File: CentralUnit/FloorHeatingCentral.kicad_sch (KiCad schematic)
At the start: 26 parts, among them J1 Screw_Terminal_01x02, J2 Conn_02x05_Odd_Even, J3 Conn_01x20, Q1 Q_NMOS_GDS, U1 ESP32-DevKitC, U2 74HC595D_118, U3 74HC595D_118, U4 RFM69-ATSHA-breakout, U5 MP1584, U6 LM1117-5.0

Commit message: More cleanup and potentially final routing
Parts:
- J2: footprint (none) -> Connector_IDC:IDC-Header_2x05_P2.54mm_Vertical
- JP1: value (none) -> Jumper_2_Open; footprint (none) -> TestPoint:TestPoint_2Pads_Pitch2.54mm_Drill0.8mm
- U2, U3: footprint digikey-footprints:SOIC-16_W3.90mm -> (none); symbol FloorHeatingCentral-rescue:74HC595D_118-dk_Logic-Shift-Registers -> 74xx:74HC595
- U4: footprint (none) -> RFM69HCW_ATSHA204A_Breakout:RFM69HCW_ATSHA204A_Breakout
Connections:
- net +24V: now also J1.2 (Pin_2); no longer J1.1 (Pin_1)
- net DL_SW: now also U1.24 (ADC2_CH2/*GPIO2); no longer U1.26 (ADC2_CH0/GPIO4)
- net GND: now also J1.1 (Pin_1); no longer J1.2 (Pin_2)
- net at U2.9 (QH'): now also U3.14 (SER)
- net ATSHA: now reaches U4.16 (ATSHA)
- net ATSHA: now also U1.26 (ADC2_CH0/GPIO4)
- no-connect marks 43 -> 42
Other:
- moved on the sheet: C1, C2, J1, U2, U3

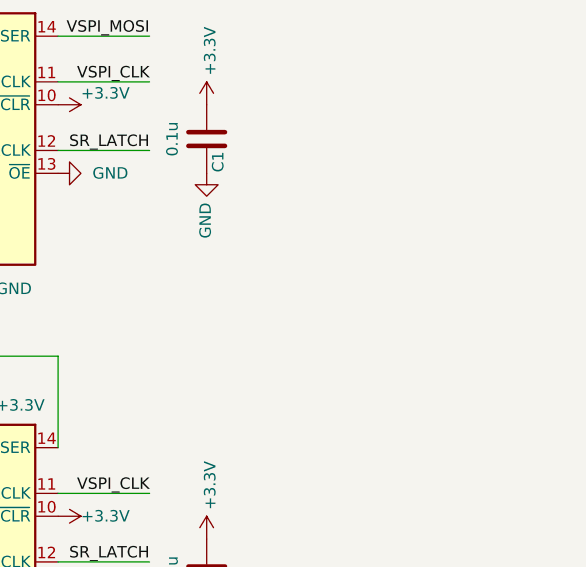
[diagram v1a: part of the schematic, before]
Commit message: Added power port for thermostats
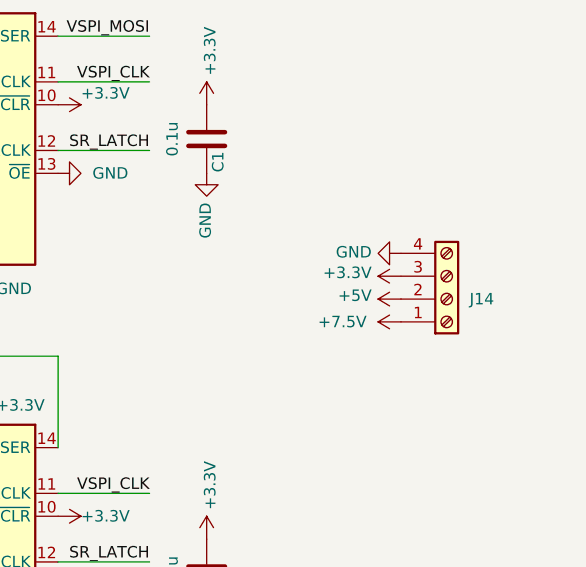
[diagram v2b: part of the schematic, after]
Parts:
- added J14: (no value), symbol Connector:Screw_Terminal_01x04
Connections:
- net +3V3: now also J14.3 (Pin_3)
- net +5V: now also J14.2 (Pin_2)
- net +7.5V: now also J14.1 (Pin_1)
- net GND: now also J14.4 (Pin_4)
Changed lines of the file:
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@@
+    (pin "1")
+  )
+  (symbol (lib_id "power:+7.5V") (at 269.24 78.74 90) (unit 1)
+    (in_bom yes) (on_board yes) (fields_autoplaced)
+    (property "Reference" "#PWR0103" (id 0) (at 273.05 78.74 0)
+      (effects (font (size 1.27 1.27)) hide)
+    )
+    (property "Value" "+7.5V" (id 1) (at 265.43 78.7399 90)
+      (effects (font (size 1.27 1.27)) (justify left))
+    )
+    (property "Footprint" "" (id 2) (at 269.24 78.74 0)
+      (effects (font (size 1.27 1.27)) hide)
+    )
+    (property "Datasheet" "" (id 3) (at 269.24 78.74 0)
+      (effects (font (size 1.27 1.27)) hide)
+    )
     (pin "1")
   )
@@
     (pin "1")
   )
+  (symbol (lib_id "power:+3.3V") (at 269.24 73.66 90) (unit 1)
+    (in_bom yes) (on_board yes)
+    (property "Reference" "#PWR0102" (id 0) (at 273.05 73.66 0)
+      (effects (font (size 1.27 1.27)) hide)
+    )
+    (property "Value" "+3.3V" (id 1) (at 265.9888 73.279 90)
+      (effects (font (size 1.27 1.27)) (justify left))
+    )
+    (property "Footprint" "" (id 2) (at 269.24 73.66 0)
+      (effects (font (size 1.27 1.27)) hide)
+    )
+    (property "Datasheet" "" (id 3) (at 269.24 73.66 0)
+      (effects (font (size 1.27 1.27)) hide)
+    )
+    (pin "1")
+  )
   (symbol (lib_id "power:GND") (at 105.41 50.8 90) (unit 1)
     (in_bom yes) (on_board yes)
@@
     (pin "1")
     (pin "2")
+  )
+  (symbol (lib_id "Connector:Screw_Terminal_01x04") (at 274.32 76.2 0) (mirror x) (unit 1)
+    (in_bom yes) (on_board yes)
+    (property "Reference" "J14" (id 0) (at 276.86 76.2001 0)
+      (effects (font (size 1.27 1.27)) (justify left))
+    )
+    (property "Value" "" (id 1) (at 260.35 68.58 0)
+      (effects (font (size 1.27 1.27)) (justify left))
+    )
+    (property "Footprint" "" (id 2) (at 274.32 76.2 0)
+      (effects (font (size 1.27 1.27)) hide)
+    )
+    (property "Datasheet" "~" (id 3) (at 274.32 76.2 0)
+      (effects (font (size 1.27 1.27)) hide)
+    )
+    (pin "1")
+    (pin "2")
+    (pin "3")
+    (pin "4")
   )
   (symbol (lib_id "power:GND") (at 45.72 154.94 0) (mirror x) (unit 1)
@@
     (pin "2")
   )
+  (symbol (lib_id "power:+5V") (at 269.24 76.2 90) (unit 1)
+    (in_bom yes) (on_board yes)
+    (property "Reference" "#PWR0104" (id 0) (at 273.05 76.2 0)
+      (effects (font (size 1.27 1.27)) hide)
+    )
+    (property "Value" "+5V" (id 1) (at 265.9888 75.819 90)
+      (effects (font (size 1.27 1.27)) (justify left))
+    )
+    (property "Footprint" "" (id 2) (at 269.24 76.2 0)
+      (effects (font (size 1.27 1.27)) hide)
+    )
+    (property "Datasheet" "" (id 3) (at 269.24 76.2 0)
+      (effects (font (size 1.27 1.27)) hide)
+    )
+    (pin "1")
+  )
   (symbol (lib_id "Regulator_Linear:LM1117-5.0") (at 266.7 151.13 0) (unit 1)
     (in_bom yes) (on_board yes) (fields_autoplaced)
@@
     )
     (property "Datasheet" "" (id 3) (at 35.56 68.58 0)
+      (effects (font (size 1.27 1.27)) hide)
+    )
+    (pin "1")
+  )
+  (symbol (lib_id "power:GND") (at 269.24 71.12 270) (mirror x) (unit 1)
+    (in_bom yes) (on_board yes)
+    (property "Reference" "#PWR0101" (id 0) (at 262.89 71.12 0)
+      (effects (font (size 1.27 1.27)) hide)
+    )
+    (property "Value" "GND" (id 1) (at 265.9888 70.993 90)
+      (effects (font (size 1.27 1.27)) (justify right))
+    )
+    (property "Footprint" "" (id 2) (at 269.24 71.12 0)
+      (effects (font (size 1.27 1.27)) hide)
+    )
+    (property "Datasheet" "" (id 3) (at 269.24 71.12 0)
       (effects (font (size 1.27 1.27)) hide)
     )
@@
       (reference "#PWR067") (unit 1) (value "GND") (footprint "")
     )
+    (path "/d850a015-18e8-4d5f-b055-62f32f0481c9"
+      (reference "#PWR0101") (unit 1) (value "GND") (footprint "")
+    )
+    (path "/4e7ee7d6-9b9d-4371-8bc3-5a8e06dcc2a1"
+      (reference "#PWR0102") (unit 1) (value "+3.3V") (footprint "")
+    )
+    (path "/16c5667a-1e78-4961-8cc8-8d83561b2a81"
+      (reference "#PWR0103") (unit 1) (value "+7.5V") (footprint "")
+    )
+    (path "/ac568034-b28c-46ea-94e2-1835bcb0f364"
+      (reference "#PWR0104") (unit 1) (value "+5V") (footprint "")
+    )
     (path "/00000000-0000-0000-0000-00005c06ccb4"
       (reference "C1") (unit 1) (value "0.1u") (footprint "Capacitor_SMD:C_1206_3216Metric")
@@
       (reference "J13") (unit 1) (value "Screw_Terminal_01x02") (footprint "TerminalBlock_Phoenix:TerminalBlock_Phoenix_MKDS-3-2-5.08_1x02_P5.08mm_Horizontal")
     )
+    (path "/7b6958bf-b22d-4d31-8fca-dc57052f646e"
+      (reference "J14") (unit 1) (value "Screw_Terminal_01x04") (footprint "TerminalBlock_Phoenix:TerminalBlock_Phoenix_MKDS-3-4-5.08_1x04_P5.08mm_Horizontal")
+    )
     (path "/7755e69f-745a-47d4-b1ef-97d3ad20f50d"

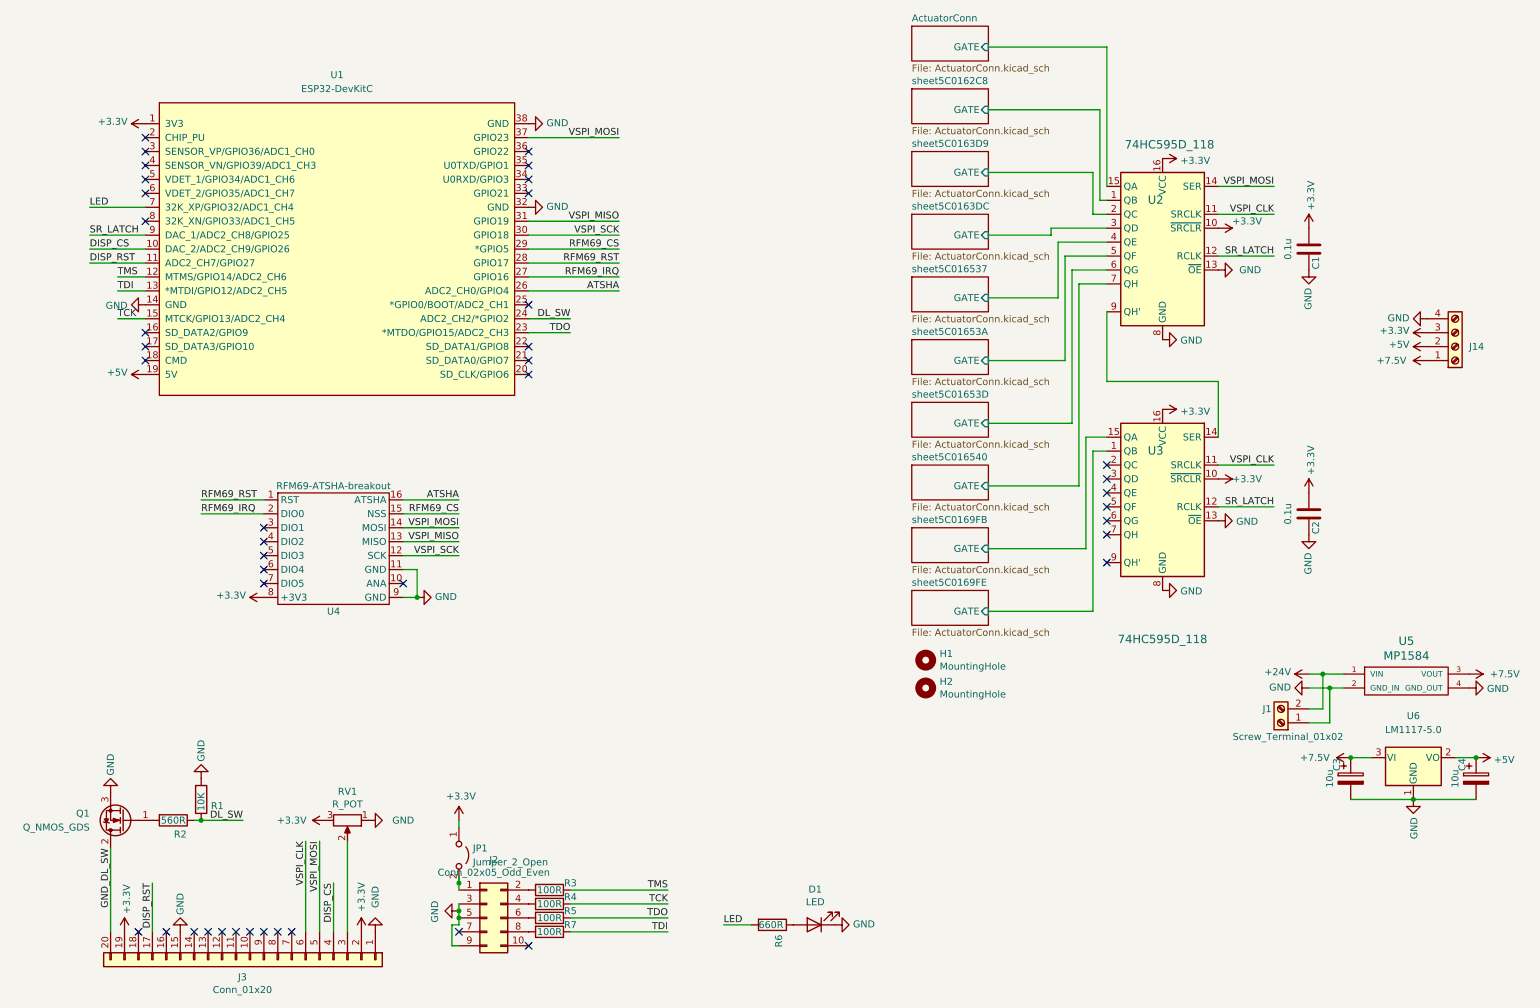
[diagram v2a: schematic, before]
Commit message: Added I2c ports. Final routing. Production.
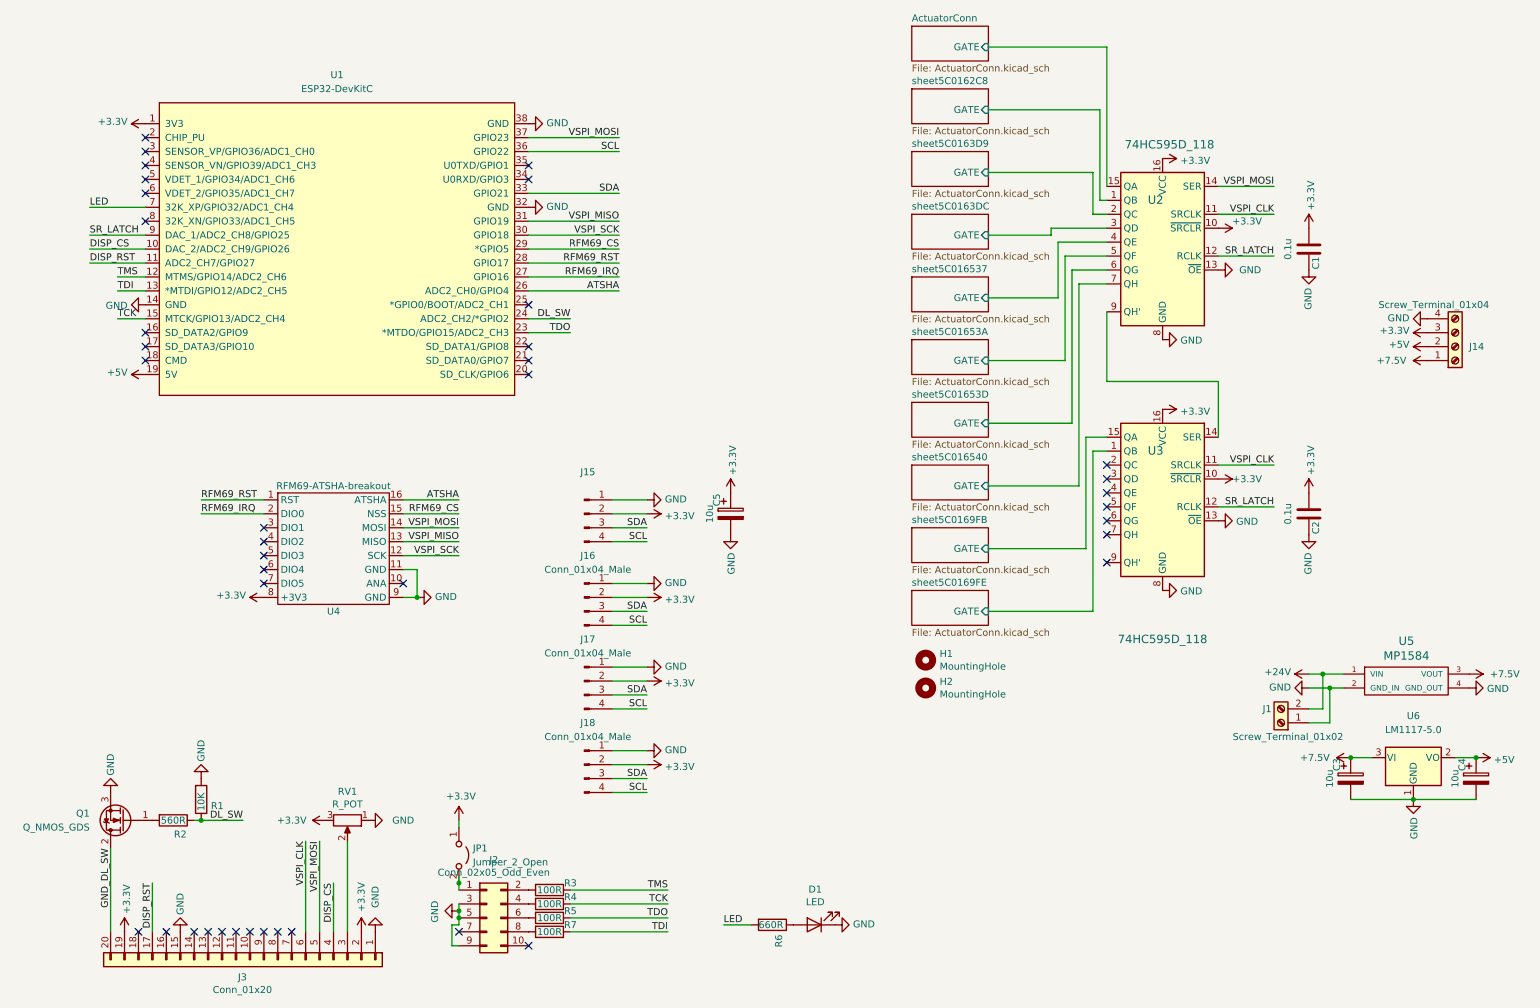
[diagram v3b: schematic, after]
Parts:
- added C5: 10u, Capacitor_Tantalum_SMD:CP_EIA-3216-18_Kemet-A, symbol Device:C_Polarized
- added J15: (no value), symbol Connector:Conn_01x04_Male
- added J16, J17, J18: Conn_01x04_Male, Connector_JST:JST_SH_BM04B-SRSS-TB_1x04-1MP_P1.00mm_Vertical, symbol Connector:Conn_01x04_Male
- J14: value (none) -> Screw_Terminal_01x04; footprint (none) -> TerminalBlock_Phoenix:TerminalBlock_Phoenix_MKDS-3-4-5.08_1x04_P5.08mm_Horizontal
- U2, U3: footprint (none) -> Package_SO:SOIC-16_3.9x9.9mm_P1.27mm
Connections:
- net +3V3: now also C5.1, J15.2 (Pin_2), J16.2 (Pin_2), J17.2 (Pin_2), J18.2 (Pin_2)
- net GND: now also C5.2, J15.1 (Pin_1), J16.1 (Pin_1), J17.1 (Pin_1), J18.1 (Pin_1)
- net SDA: now reaches U1.33 (GPIO21)
- net SDA: now also J15.3 (Pin_3), J16.3 (Pin_3), J17.3 (Pin_3), J18.3 (Pin_3)
- net SCL: now reaches U1.36 (GPIO22)
- net SCL: now also J15.4 (Pin_4), J16.4 (Pin_4), J17.4 (Pin_4), J18.4 (Pin_4)
- no-connect marks 42 -> 40

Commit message: Updates
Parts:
- J15: value (none) -> Conn_01x04_Male; footprint (none) -> Connector_JST:JST_SH_BM04B-SRSS-TB_1x04-1MP_P1.00mm_Vertical
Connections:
- net VSPI_CLK is gone; now on net VSPI_SCK: J3.6 (Pin_6), U2.11 (SRCLK), U3.11 (SRCLK)
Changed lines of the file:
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@@
     (effects (font (size 1.27 1.27)) (justify right bottom))
   )
-  (label "VSPI_CLK" (at 241.3 97.79 180)
-    (effects (font (size 1.27 1.27)) (justify right bottom))
-  )
-  (label "VSPI_CLK" (at 241.3 52.07 180)
+  (label "VSPI_SCK" (at 241.3 97.79 180)
+    (effects (font (size 1.27 1.27)) (justify right bottom))
+  )
+  (label "VSPI_SCK" (at 241.3 52.07 180)
     (effects (font (size 1.27 1.27)) (justify right bottom))
   )
@@
     (effects (font (size 1.27 1.27)) (justify right bottom))
   )
-  (label "VSPI_CLK" (at 64.77 166.37 270)
+  (label "VSPI_SCK" (at 64.77 166.37 270)
     (effects (font (size 1.27 1.27)) (justify right bottom))
   )
@@
     (in_bom yes) (on_board yes) (fields_autoplaced)
     (property "Reference" "J15" (id 0) (at 116.205 99.06 0))
-    (property "Value" "" (id 1) (at 116.205 101.6 0))
-    (property "Footprint" "" (id 2) (at 115.57 106.68 0)
-      (effects (font (size 1.27 1.27)) hide)
-    )
+    (property "Value" "Conn_01x04_Male" (id 1) (at 116.205 101.6 0))
+    (property "Footprint" "Connector_JST:JST_SH_BM04B-SRSS-TB_1x04-1MP_P1.00mm_Vertical" (id 2) (at 115.57 106.68 0)
+      (effects (font (size 1.27 1.27)) hide)
+    )
